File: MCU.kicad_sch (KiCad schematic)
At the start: 29 parts, among them J7 Conn_01x04, J8 PinHeader_2x5_P1.27mm_SMD, SW1 SW_KSC441J70SHLFS_SMD, SW2 SW_KSC441J70SHLFS_SMD, U3 STM32U585CIT3, Y1 Oscillator_40MHz_YIC_OSC-S5

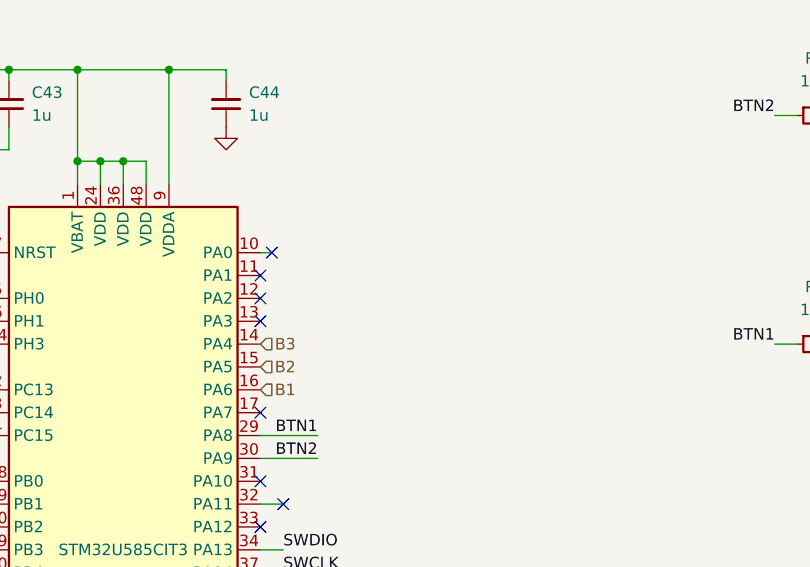
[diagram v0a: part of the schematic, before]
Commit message: Add resistor divider to the ADC input
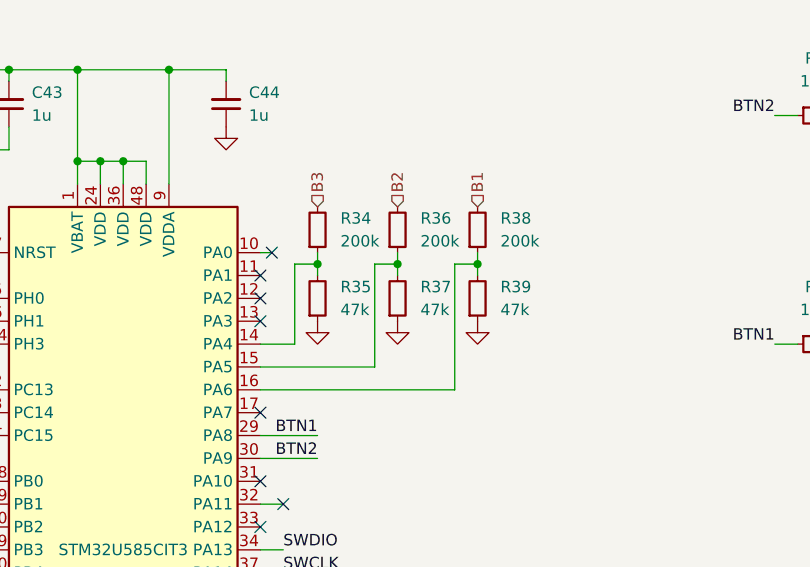
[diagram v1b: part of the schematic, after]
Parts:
- added R34, R36, R38: R_200k_0402, Hardware Components Footprints:R_0402_1005Metric, symbol Hardware Components:R_200k_0402
- added R35, R37, R39: R_47k_0402, Hardware Components Footprints:R_0402_1005Metric, symbol Hardware Components:R_47k_0402
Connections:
- net B1: now also R38.2; no longer U3.16 (PA6)
- net B2: now also R36.2; no longer U3.15 (PA5)
- net B3: now also R34.2; no longer U3.14 (PA4)
- net GND: now also R35.1, R37.1, R39.1
- new net: R34.1, R35.2, U3.14 (PA4)
- new net: R38.1, R39.2, U3.16 (PA6)
- new net: R36.1, R37.2, U3.15 (PA5)
